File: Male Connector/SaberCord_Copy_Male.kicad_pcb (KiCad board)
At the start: 2 copper layers, 29.8 x 20.3 mm, 6 parts, among them J1 Conn_02x07_Row_Letter_Last, J2 Conn_02x12_Row_Letter_Last

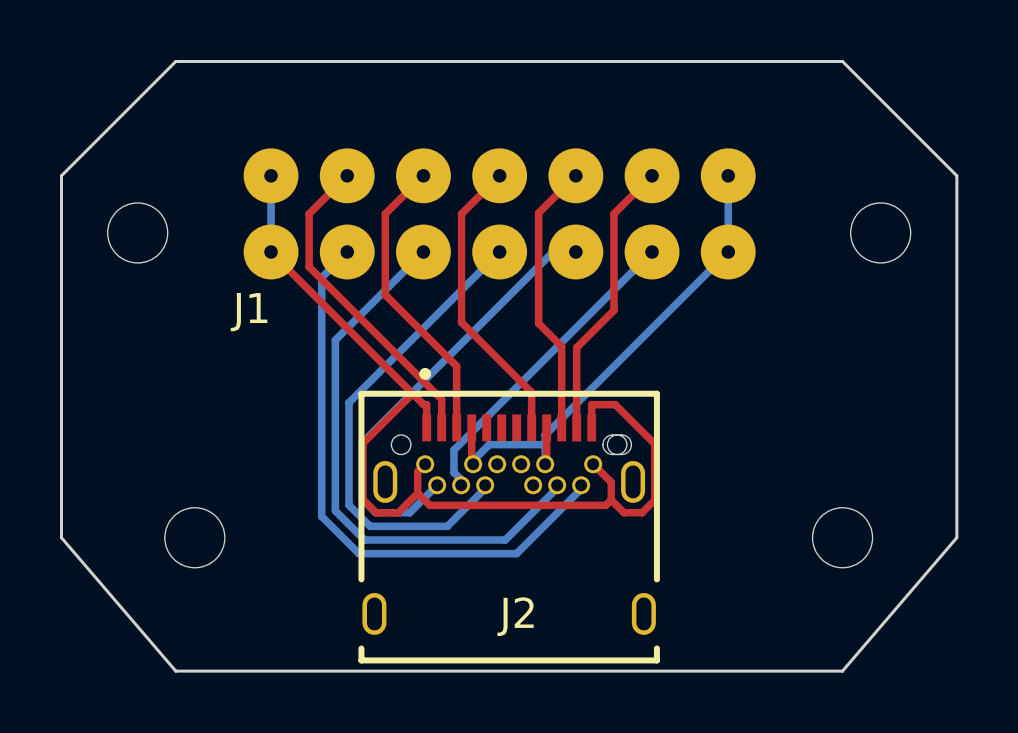
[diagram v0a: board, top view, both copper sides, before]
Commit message: organize files into parts
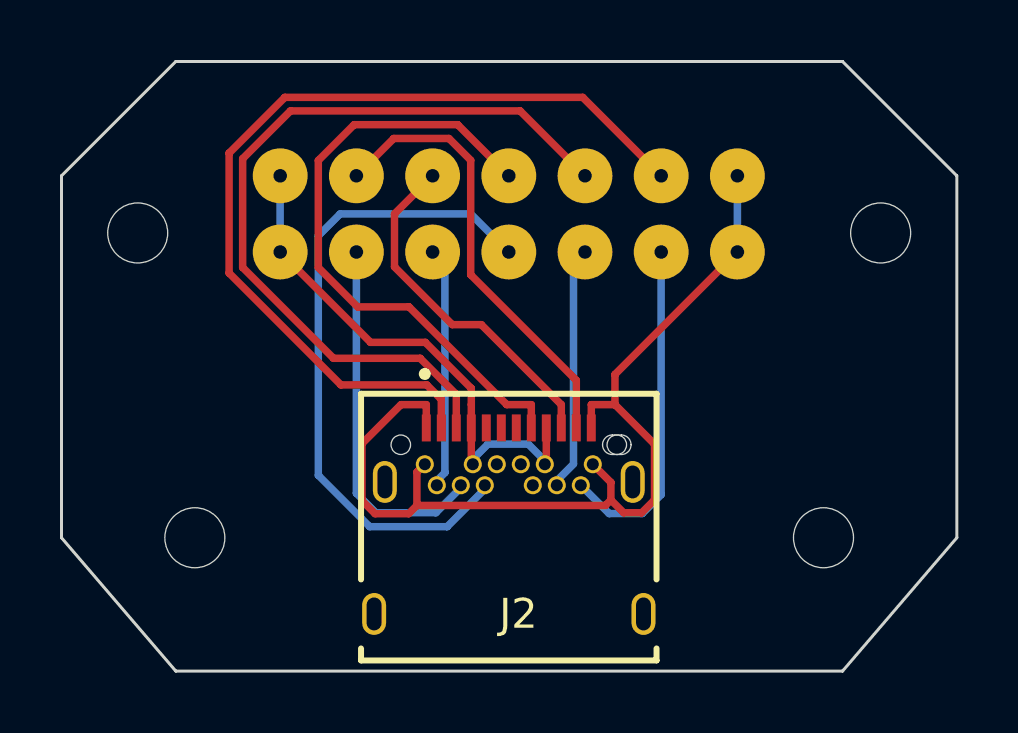
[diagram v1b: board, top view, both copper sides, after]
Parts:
- J1: moved to B.Cu
- moved bottom_right 0.63 mm to (150.5, 91.4)
- moved J1 0.31 mm to (140.0, 83.8), turned to 180 degrees
- renumbered REF** to bottom_left, REF** to bottom_right, REF** to top_left, REF** to top_right
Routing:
- net /CAN0_H: track 10.8 -> 30.0 mm
- net /CAN0_L: track 9.92 -> 26.6 mm
- net /SBU1: track 9.90 -> 20.9 mm
- net /CAN2_L: track 18.5 -> 8.16 mm
- net /CAN2_H: track 19.3 -> 11.4 mm
- net /CAN3_H: track 14.7 -> 8.06 mm
- net /SBU2: track 16.0 -> 22.1 mm
- net /CAN1_H: track 9.45 -> 15.0 mm
- net /CAN1_L: track 9.24 -> 11.8 mm
- net /CAN3_L: track 10.6 -> 12.2 mm
